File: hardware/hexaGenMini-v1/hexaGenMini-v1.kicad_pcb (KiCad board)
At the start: 2 copper layers, 58.5 x 52 mm, 72 parts, among them J1 Conn_Coaxial, J2 Conn_Coaxial, J3 Conn_01x03_Pin, J4 USB_C_Receptacle_USB2.0_16P, SW1 SW_Push, SW2 SW_Push, U1 AMS1117-3.3, U2 RP2040, U3 AD9850, U4 TPD2EUSB30, U5 W25Q128JVS, Y1 12MHz 18pF, Y2 XO53

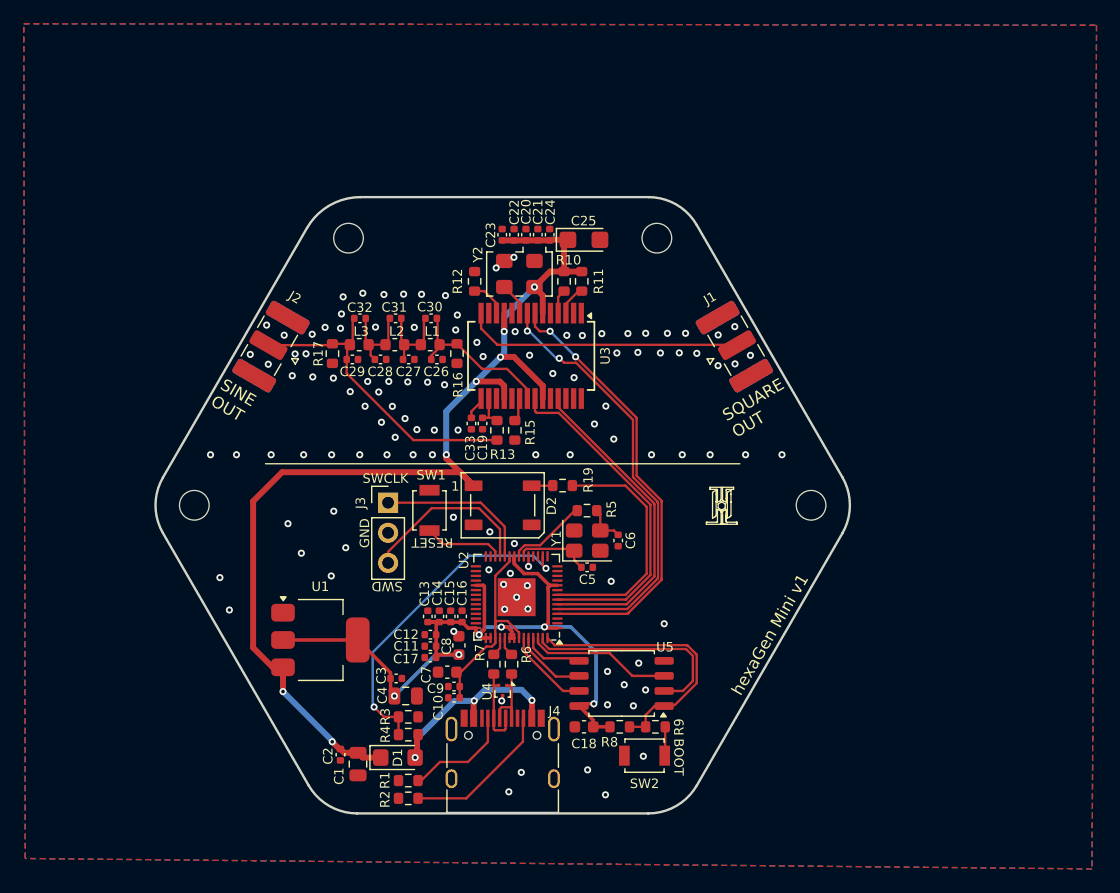
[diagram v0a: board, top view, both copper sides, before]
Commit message: fix(hotfix): basic fix
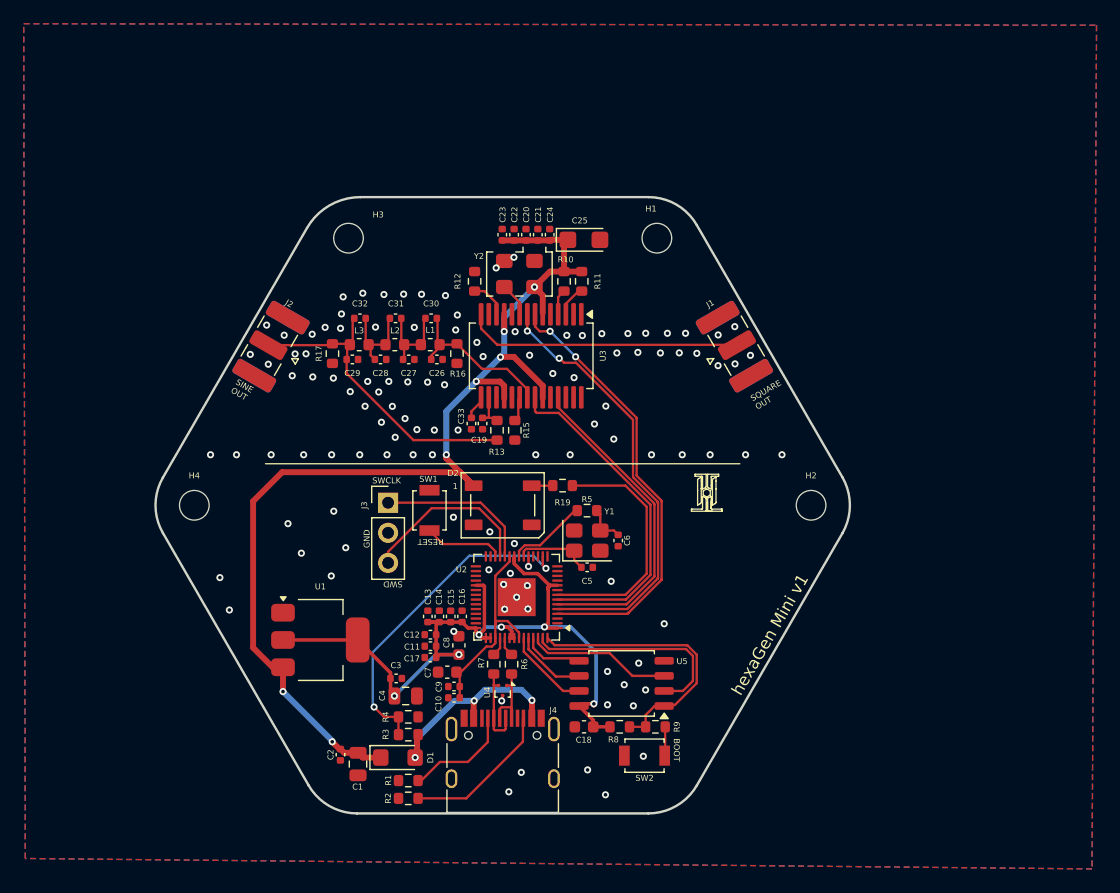
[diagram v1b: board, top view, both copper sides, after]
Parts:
- J3: footprint Connector_PinHeader_2.54mm:PinHeader_1x03_P2.54mm_Vertical -> PCB_Library:PinHeader_1x03_P2.54mm_Vertical
- J4: footprint Connector_USB:USB_C_Receptacle_HRO_TYPE-C-31-M-12 -> PCB_Library:USB_C_Receptacle_HRO_TYPE-C-31-M-12
